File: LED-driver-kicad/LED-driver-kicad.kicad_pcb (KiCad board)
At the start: 2 copper layers, 172 parts, among them J1 ARJM11C7-114-BA-EW2, J2 Conn_01x05_Socket, J3 Conn_01x02_Socket, Q1 Q_NMOS_GDS, Q2 Q_NMOS_GDS, Q3 Q_NMOS_GDS, Q4 Q_NMOS_GDS, Q5 Q_NMOS_GDS, Q6 Q_NMOS_GDS, SW1 SW_SPDT, U1 ENC28J60x-SO, U10 MIC3205YML-TR, U11 74AHC1G14, U12 MIC3205YML-TR, U2 PD70210A, U3 LV2862XLVDDCR, U4 LV2862XLVDDCR, U5 PIC16F18026-ISL, U6 MIC3205YML-TR, U7 MIC3205YML-TR, U8 MIC3205YML-TR, U9 MIC3205YML-TR, Y1 25MHz

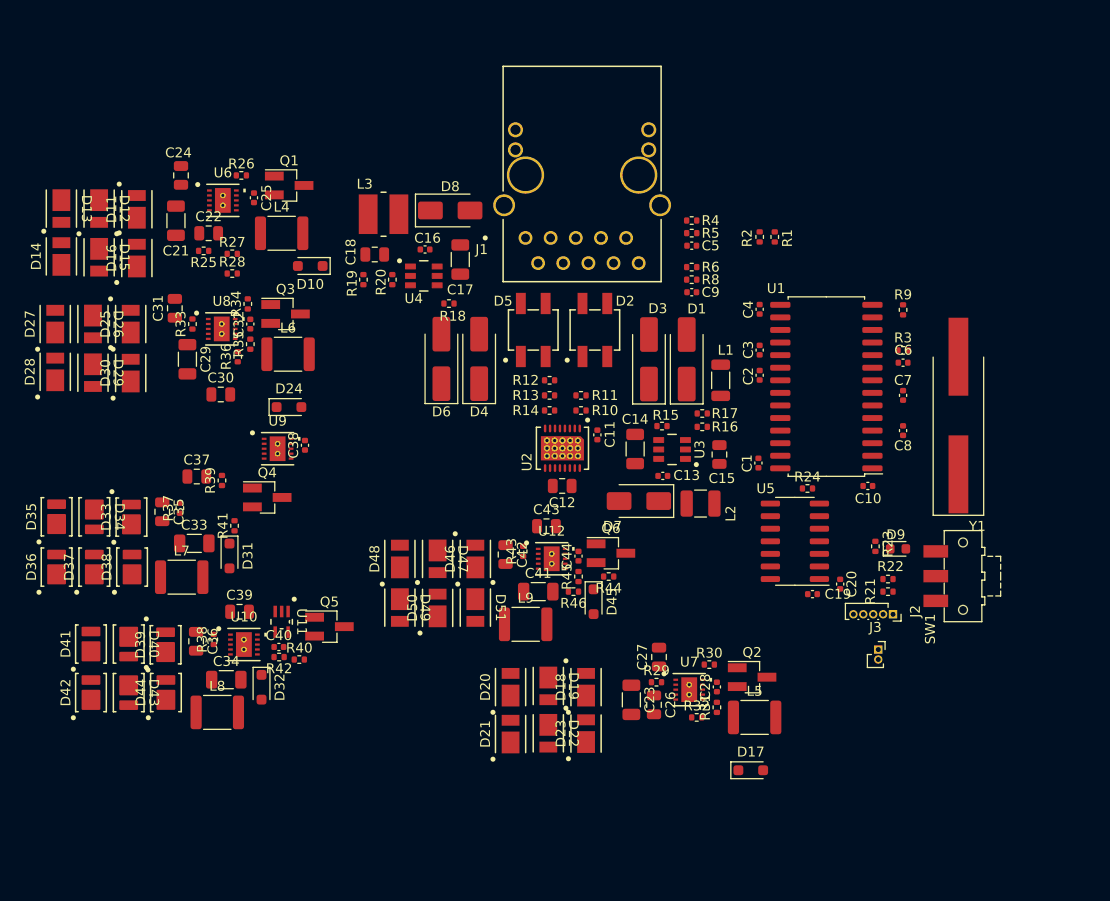
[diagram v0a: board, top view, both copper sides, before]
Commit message: update initial components layout
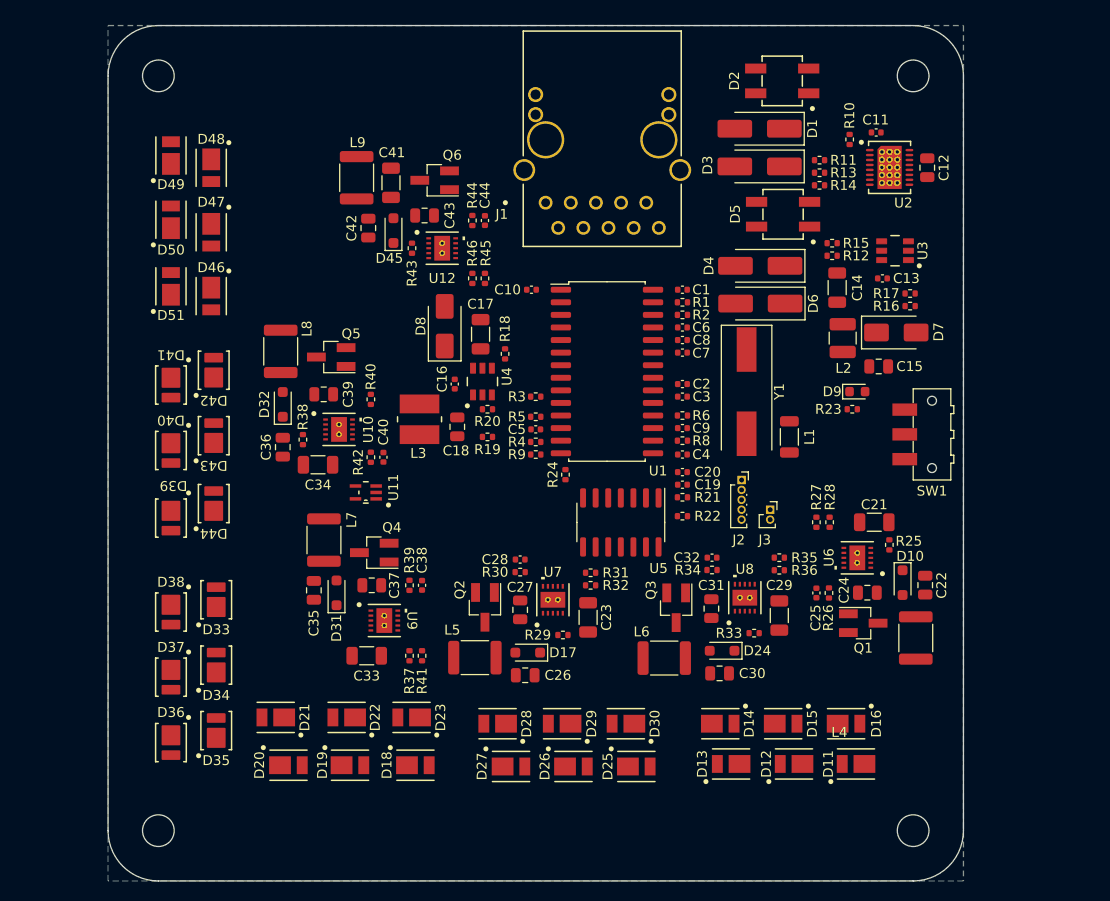
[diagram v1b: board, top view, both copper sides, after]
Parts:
- added H1: MountingHole, MountingHole:MountingHole_3.2mm_M3, F.Cu at (76.2, 50.8)
- added H2: MountingHole, MountingHole:MountingHole_3.2mm_M3, F.Cu at (152.4, 50.8)
- added H3: MountingHole, MountingHole:MountingHole_3.2mm_M3, F.Cu at (152.4, 127.0)
- added H4: MountingHole, MountingHole:MountingHole_3.2mm_M3, F.Cu at (76.2, 127.0)
- Y1: footprint Crystal:Crystal_SMD_HC49-SD_HandSoldering -> Crystal:Crystal_SMD_HC49-SD
- moved D11 91.7 mm to (146.6, 120.3), turned to 180 degrees
- moved D12 89.8 mm to (140.4, 120.3), turned to 180 degrees
- moved D13 87.8 mm to (134.0, 120.3), turned to 180 degrees
- moved D16 85.7 mm to (145.6, 116.2), turned to 0 degrees
- moved D15 83.6 mm to (139.3, 116.2), turned to 0 degrees
- moved D14 81.6 mm to (132.9, 116.2), turned to 0 degrees
- moved C24 81.1 mm to (147.8, 103.0), turned to 180 degrees
- moved C22 80.6 mm to (153.6, 102.2), turned to -90 degrees
- moved C21 76.8 mm to (148.5, 95.9), turned to 0 degrees
- moved L4 75.9 mm to (152.7, 107.5), turned to 90 degrees
- moved R25 75.3 mm to (150.0, 98.2), turned to -90 degrees
- moved U6 73.5 mm to (146.8, 99.5), turned to 180 degrees
- moved Q1 72.9 mm to (147.4, 106.1)
- moved R26 72.8 mm to (143.9, 103.0), turned to -90 degrees
- moved C25 69.4 mm to (142.6, 103.0)
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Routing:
- added copper zone on B.Cu, net GND
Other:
- board outline added: 86.4 x 86.4 mm

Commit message: update PCB traces and planes
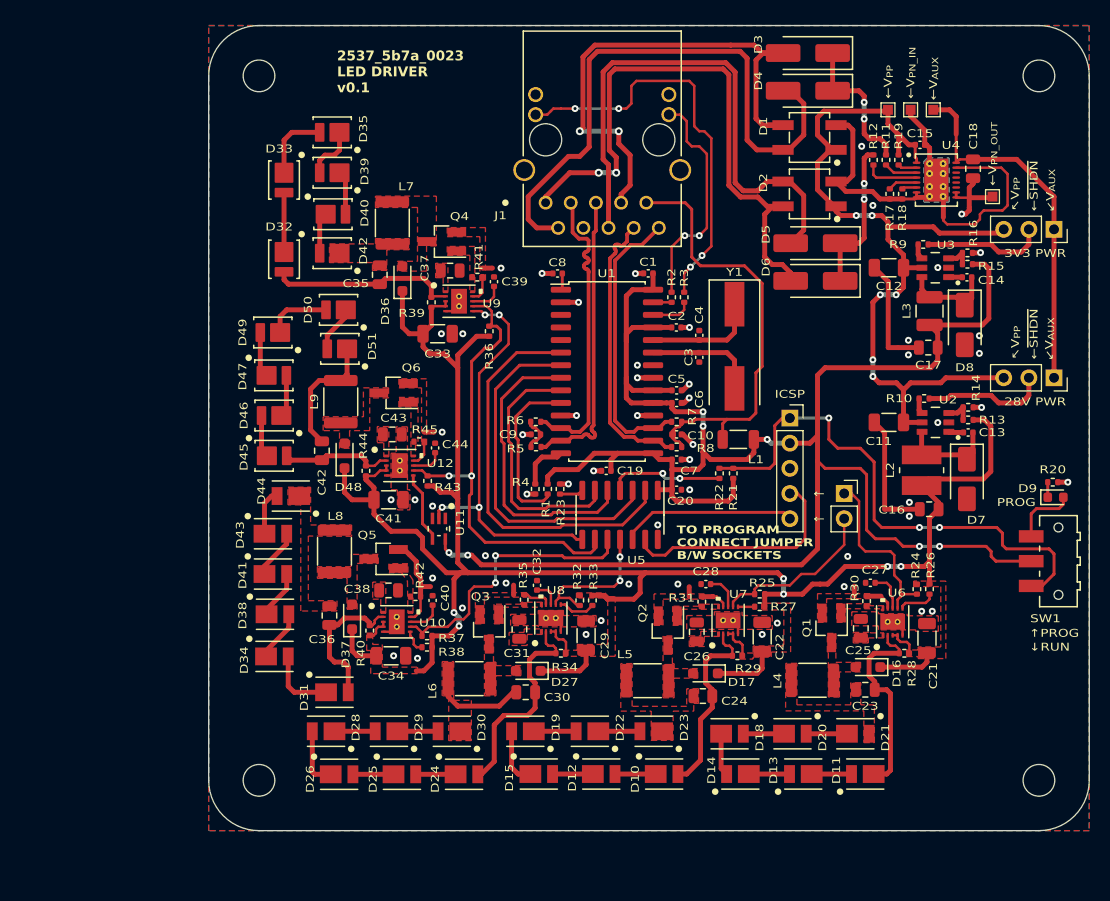
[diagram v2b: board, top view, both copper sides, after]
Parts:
- added J2: Conn_01x03_Socket, Connector_PinSocket_2.54mm:PinSocket_1x03_P2.54mm_Vertical, F.Cu at (166.6, 66.3)
- added J3: Conn_01x03_Socket, Connector_PinSocket_2.54mm:PinSocket_1x03_P2.54mm_Vertical, F.Cu at (166.6, 81.3)
- added NT1: NetTie_2, NetTie:NetTie-2_SMD_Pad0.5mm, F.Cu at (150.0, 94.5)
- added NT10: NetTie_2, NetTie:NetTie-2_SMD_Pad0.5mm, F.Cu at (103.5, 86.8)
- added NT2: NetTie_2, NetTie:NetTie-2_SMD_Pad0.5mm, F.Cu at (150.4, 78.2)
- added NT3: NetTie_2, NetTie:NetTie-2_SMD_Pad0.5mm, F.Cu at (155.5, 64.6)
- added NT4: NetTie_2, NetTie:NetTie-2_SMD_Pad0.5mm, F.Cu at (158.1, 63.6)
- added NT5: NetTie_2, NetTie:NetTie-2_SMD_Pad0.5mm, F.Cu at (129.8, 102.9)
- added NT6: NetTie_2, NetTie:NetTie-2_SMD_Pad0.5mm, F.Cu at (146.5, 102.8)
- added NT7: NetTie_2, NetTie:NetTie-2_SMD_Pad0.5mm, F.Cu at (112.1, 102.7)
- added NT8: NetTie_2, NetTie:NetTie-2_SMD_Pad0.5mm, F.Cu at (103.2, 102.4)
- added NT9: NetTie_2, NetTie:NetTie-2_SMD_Pad0.5mm, F.Cu at (109.4, 70.2)
- added TP1: TestPoint, TestPoint:TestPoint_Pad_1.0x1.0mm, F.Cu at (149.9, 54.2)
- added TP2: TestPoint, TestPoint:TestPoint_Pad_1.0x1.0mm, F.Cu at (152.1, 54.2)
- added TP3: TestPoint, TestPoint:TestPoint_Pad_1.0x1.0mm, F.Cu at (154.4, 54.2)
- added TP4: TestPoint, TestPoint:TestPoint_Pad_1.0x1.0mm, F.Cu at (160.4, 63.0)
- J4: renamed from J2; footprint Connector_PinSocket_1.00mm:PinSocket_1x05_P1.00mm_Vertical -> Connector_PinSocket_2.54mm:PinSocket_1x05_P2.54mm_Vertical
- J5: renamed from J3; footprint Connector_PinSocket_1.00mm:PinSocket_1x02_P1.00mm_Vertical -> Connector_PinSocket_2.54mm:PinSocket_1x02_P2.54mm_Vertical
- R18: renamed from R14; value 30.9 -> 30R9
- moved D35 61.5 mm to (93.8, 56.5), turned to 180 degrees
- moved D39 59.8 mm to (93.8, 60.6), turned to 180 degrees
- moved D7 54.9 mm to (157.8, 91.5), turned to -90 degrees
- moved C13 52.1 mm to (158.0, 86.8), turned to 0 degrees
- moved L2 50.9 mm to (153.3, 90.6)
- moved D40 49.5 mm to (93.8, 64.8), turned to 0 degrees
- moved D33 49.5 mm to (88.9, 61.3), turned to -90 degrees
- moved R13 48.6 mm to (158.0, 85.5), turned to 180 degrees
- moved R14 48.5 mm to (158.0, 84.3), turned to 0 degrees
- moved C16 48.4 mm to (154.0, 94.5), turned to 180 degrees
- moved C34 47.8 mm to (99.7, 109.3), turned to 0 degrees
- moved U2 45.9 mm to (154.7, 85.8), turned to 180 degrees
- moved D38 45.5 mm to (88.0, 105.2), turned to 0 degrees
- moved D41 43.5 mm to (87.8, 101.1), turned to 0 degrees
- moved D34 43.3 mm to (87.9, 109.4), turned to 0 degrees
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- renumbered C9 to C10, C17 to C11, C14 to C12, C16 to C13, C13 to C14, C11 to C15, C18 to C16, C15 to C17, C12 to C18, C20 to C19, C6 to C2, C19 to C20, C29 to C22, C22 to C23, C30 to C24, C24 to C25, C31 to C26, C25 to C27, C32 to C28, C23 to C29, C7 to C3, C26 to C30, C27 to C31, C28 to C32, C41 to C34, C42 to C36, C43 to C38, C38 to C39, C8 to C4, C44 to C40, C34 to C41, C36 to C42, C39 to C43, C40 to C44, C2 to C5, C3 to C6, C4 to C7, C10 to C8, C5 to C9, D2 to D1, D25 to D10, D26 to D12, D12 to D13, D13 to D14, D27 to D15, D10 to D16, D24 to D17, D14 to D18, D28 to D19, D5 to D2, D15 to D20, D16 to D21, D29 to D22, D30 to D23, D18 to D24, D19 to D25, D20 to D26, D17 to D27, D21 to D28, D22 to D29, D1 to D3, D23 to D30, D46 to D31, D33 to D32, D34 to D33, D47 to D34, D31 to D36, D45 to D37, D48 to D38, D36 to D39, D3 to D4, D37 to D40, D49 to D41, D38 to D42, D50 to D43, D51 to D44, D39 to D45, D40 to D46, D41 to D47, D32 to D48, D42 to D49, D4 to D5, D43 to D50, D44 to D51, D8 to D7, D7 to D8, L3 to L2, L2 to L3, L6 to L5, L5 to L6, L9 to L8, L8 to L9, Q3 to Q2, Q2 to Q3, Q6 to Q5, Q5 to Q6, R3 to R1, R18 to R10, R19 to R13, R20 to R14, R16 to R15, R17 to R16, R13 to R17, R10 to R19, R1 to R2, R23 to R20, R24 to R23, R27 to R24, R35 to R25, R28 to R26, R36 to R27, R25 to R28, R33 to R29, R2 to R3, R26 to R30, R34 to R31, R31 to R32, R32 to R33, R29 to R34, R30 to R35, R41 to R36, R45 to R37, R46 to R38, R37 to R39, R9 to R4, R43 to R40, R39 to R41, R44 to R42, R42 to R43, R38 to R44, R40 to R45, R4 to R5, R5 to R6, R6 to R7, R15 to R9, U12 to U10, U10 to U12, U4 to U2, U2 to U4, U8 to U7, U7 to U8
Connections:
- net /Power/DCDC_EN renamed /Power/VAUX
- C11 pad 1: /Power/VPPo -> /Power/VPP
- C11 pad 2: GND -> /Power/28V_C_{IN}_GND
- C12 pad 1: /Power/VPPo -> /Power/VPP
- C12 pad 2: GND -> /Power/3V3_C_{IN}_GND
- C15 pad 1: /Power/VPPo -> /Power/VPP
- C15 pad 2: /Power/WA_EN -> /Power/VPN_IN
- C18 pad 2: GND -> /Power/VPN_OUT
- D1 pad 1: /Power/VPPo -> /Power/VPP
- D1 pad 3: /Power/WA_EN -> /Power/VPN_IN
- D2 pad 1: /Power/VPPo -> /Power/VPP
- D2 pad 3: /Power/WA_EN -> /Power/VPN_IN
- Q1 pad 3: GND -> /LEDs/PGND_RED
- Q2 pad 3: GND -> /LEDs/PGND_GREEN
- Q3 pad 3: GND -> /LEDs/PGND_BLUE
- Q4 pad 3: GND -> /LEDs - amber and white/PGND_WHITE
- Q5 pad 3: GND -> /LEDs - amber and white/PGND_AMBER
- Q6 pad 3: GND -> /LEDs - amber and white/PGND_WHITE_P
- R10 pad 1: /Power/VPPo -> Net-(U2-~{SHDN})
- R10 pad 2: Net-(U4-~{SHDN}) -> /Power/28V_~{SHDN}
- R17 pad 2: /Power/WA_EN -> /Power/VPN_IN
- R18 pad 2: /Power/WA_EN -> /Power/VPN_IN
- R19 pad 1: /Power/VPPo -> /Power/VPP
- R30 pad 2: GND -> /LEDs/PGND_RED
- R31 pad 2: GND -> /LEDs/PGND_GREEN
- R35 pad 2: GND -> /LEDs/PGND_BLUE
- R41 pad 2: GND -> /LEDs - amber and white/PGND_WHITE
- R42 pad 2: GND -> /LEDs - amber and white/PGND_AMBER
- R45 pad 2: GND -> /LEDs - amber and white/PGND_WHITE_P
- R9 pad 1: /Power/VPPo -> Net-(U3-~{SHDN})
- R9 pad 2: Net-(U3-~{SHDN}) -> /Power/3V3_~{SHDN}
- U10 pad 9: GND -> /LEDs - amber and white/PGND_AMBER
- U11 pad 1: (no net) -> unconnected-(U11-NC-Pad1)
- U12 pad 9: GND -> /LEDs - amber and white/PGND_WHITE_P
- U2 pad 4: Net-(U4-~{SHDN}) -> Net-(U2-~{SHDN})
- U2 pad 5: /Power/VPPo -> /Power/VPP
- U3 pad 5: /Power/VPPo -> /Power/VPP
- U4 pad 1: /Power/VPPo -> /Power/VPP
- U4 pad 10: GND -> /Power/VPN_OUT
- U4 pad 17: /Power/WA_EN -> /Power/VPN_IN
- U4 pad 7: /Power/WA_EN -> /Power/VPN_IN
- U4 pad 8: /Power/WA_EN -> /Power/VPN_IN
- U4 pad 9: GND -> /Power/VPN_OUT
- U6 pad 9: GND -> /LEDs/PGND_RED
- U7 pad 9: GND -> /LEDs/PGND_GREEN
- U8 pad 9: GND -> /LEDs/PGND_BLUE
- U9 pad 9: GND -> /LEDs - amber and white/PGND_WHITE
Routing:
- net +28V: track 0.00 -> 207.0 mm, vias 0 -> 6
- net +3.3V: track 0.00 -> 204.0 mm, vias 0 -> 7
- net /Power/VPP: track 0.00 -> 86.4 mm, vias 0 -> 6
- net RJ45_VC1-: track 0.00 -> 60.1 mm
- net RJ45_VC2-: track 0.00 -> 59.6 mm, vias 0 -> 2
- net RJ45_VC2+: track 0.00 -> 54.9 mm
- net /Microcontroller/MCU_ICSP_MCLR: track 0.00 -> 54.3 mm, vias 0 -> 3
- net RJ45_VC1+: track 0.00 -> 54.2 mm, vias 0 -> 2
- net MCU_CCP1: track 0.00 -> 47.7 mm, vias 0 -> 2
- net /Ethernet/RJ45_TCT: track 0.00 -> 45.0 mm
- net /Ethernet/RJ45_LED_R_ANODE: track 0.00 -> 41.7 mm, vias 0 -> 4
- net MCU_WHITE_LED: track 0.00 -> 41.4 mm, vias 0 -> 4
- net MCU_SPI_SDI/MOSI: track 0.00 -> 40.6 mm
- net /Power/VAUX: track 0.00 -> 37.1 mm
- net MCU_SPI_SDO/MISO: track 0.00 -> 35.8 mm
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- added copper zone on F.Cu, net +28V
- added copper zone on F.Cu, net /LEDs - amber and white/PGND_WHITE
- added copper zone on F.Cu, net /LEDs - amber and white/PGND_WHITE_P
- added copper zone on F.Cu, net /LEDs/PGND_BLUE
- added copper zone on F.Cu, net /LEDs/PGND_GREEN
- added copper zone on F.Cu, net /LEDs/PGND_RED
- added copper zone on B.Cu, net /Power/VPN_IN
- added copper zone on F.Cu, net GND
- added copper zone on F.Cu, net Net-(D16-A)
- added copper zone on F.Cu, net Net-(D17-A)
- added copper zone on F.Cu, net Net-(D21-K)
- added copper zone on F.Cu, net Net-(D23-K)
- added copper zone on F.Cu, net Net-(D27-A)
- added copper zone on F.Cu, net Net-(D30-K)
- added copper zone on F.Cu, net Net-(D36-A)
- added copper zone on F.Cu, net Net-(D37-A)
- added copper zone on F.Cu, net Net-(D42-K)
- added copper zone on F.Cu, net Net-(D44-K)
- added copper zone on F.Cu, net Net-(D48-A)
- added copper zone on F.Cu, net Net-(Q1-G)
- added copper zone on F.Cu, net Net-(Q2-G)
- added copper zone on F.Cu, net Net-(Q3-G)
- added copper zone on F.Cu, net Net-(Q4-G)
- added copper zone on F.Cu, net Net-(Q5-G)
- added copper zone on F.Cu, net Net-(Q6-G)
- added copper zone on F.Cu, net Net-(U10-VCC)
- added copper zone on F.Cu, net Net-(U12-VCC)
- added copper zone on F.Cu, net Net-(U6-VCC)
- added copper zone on F.Cu, net Net-(U7-VCC)
- added copper zone on F.Cu, net Net-(U8-VCC)
- added copper zone on F.Cu, net Net-(U9-VCC)
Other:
- board size 86.4 x 86.4 mm -> 88.9 x 81.3 mm
- board text added: "2537_5b7a_0023 LED DRIVER v0.1"
- board text added: "TO PROGRAM CONNECT JUMPER B/W SOCKETS"
